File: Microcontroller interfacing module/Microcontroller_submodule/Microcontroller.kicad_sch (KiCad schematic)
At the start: 7 parts, among them U1 STM32F051C6Tx, Y1 8MHz

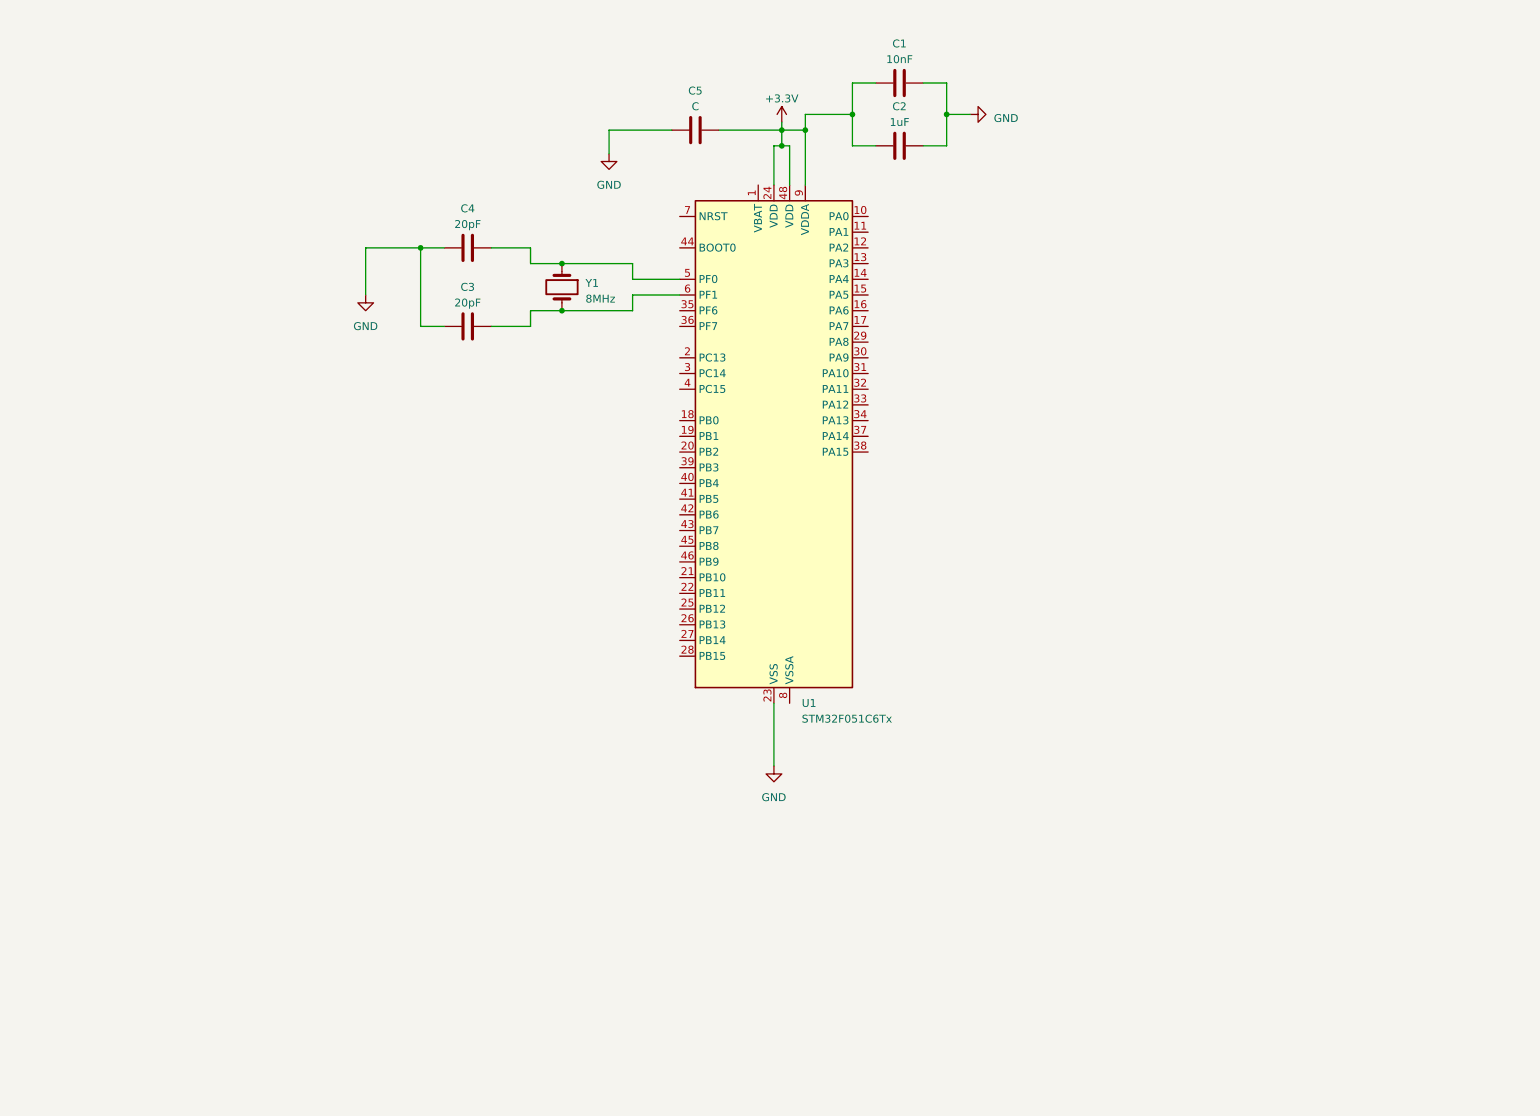
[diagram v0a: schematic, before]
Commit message: Assignment 2 microcontroller sub-module complete
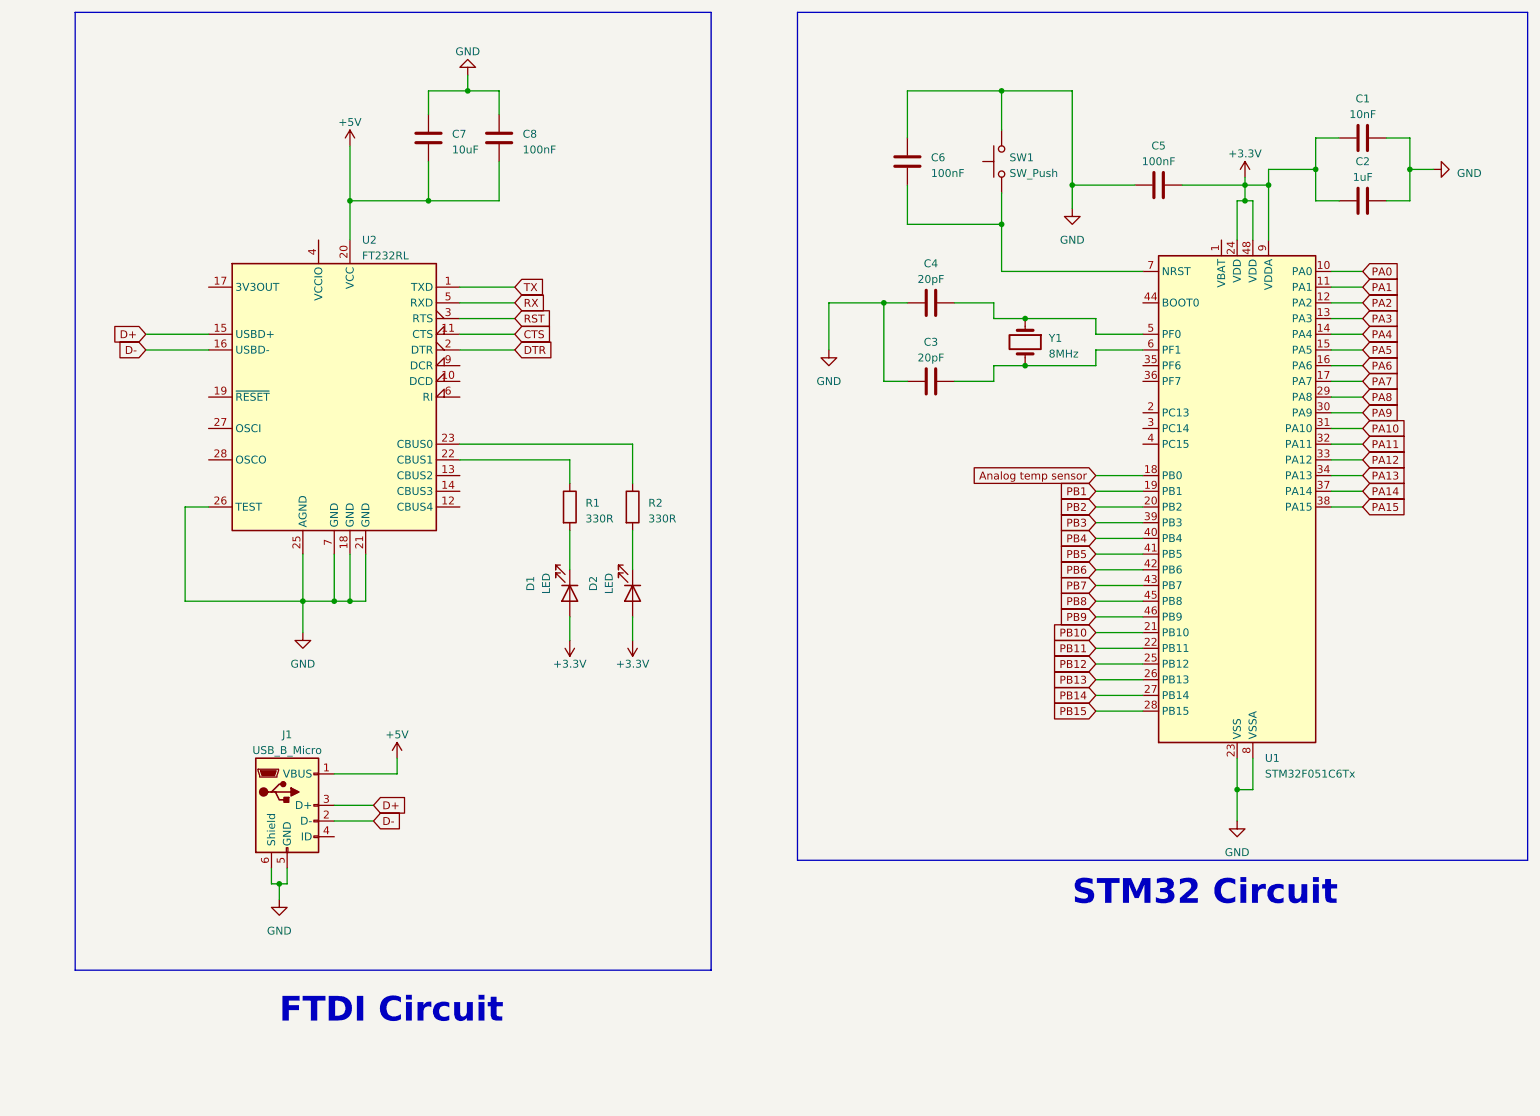
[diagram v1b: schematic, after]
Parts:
- added C6, C8: 100nF, symbol Device:C
- added C7: 10uF, symbol Device:C
- added D1, D2: LED, symbol Device:LED
- added J1: USB_B_Micro, symbol Connector:USB_B_Micro
- added R1, R2: 330R, symbol Device:R
- added SW1: SW_Push, symbol Switch:SW_Push
- added U2: FT232RL, Package_SO:SSOP-28_5.3x10.2mm_P0.65mm, symbol Interface_USB:FT232RL
- C1: Extended part (none) -> 0; JLCPCB Part no: (none) -> C49678; Package (none) -> 0805; Price per unit (none) -> 0.0046; Total price (none) -> 0.0046
- C2: Extended part (none) -> 0; JLCPCB Part no: (none) -> C28323; Package (none) -> 0805; Price per unit (none) -> 0.0087; Total price (none) -> 0.0087
- C3, C4: Extended part (none) -> 0; JLCPCB Part no: (none) -> C107145; Package (none) -> 0805; Price per unit (none) -> 0.0059; Total price (none) -> 0.0118
- C5: value C -> 100nF; Extended part (none) -> 0; JLCPCB Part no: (none) -> C49678; Package (none) -> 0805; Price per unit (none) -> 0.0046; Total price (none) -> 0.0138
- Y1: Extended part (none) -> 0; JLCPCB Part no: (none) -> C12674; Package (none) -> SMD; Price per unit (none) -> 0.0864; Total price (none) -> 0.0864
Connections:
- net +3.3V: now also D1.2 (A), D2.2 (A)
- net GND: now also U1.8 (VSSA), C6.1, C7.1, C8.1, J1.5 (GND), J1.6 (Shield), SW1.2, U2.18 (GND), U2.21 (GND), U2.25 (AGND), U2.26 (TEST), U2.7 (GND)
- net PA0: now reaches U1.10 (PA0)
- net PA1: now reaches U1.11 (PA1)
- net PA2: now reaches U1.12 (PA2)
- net PA3: now reaches U1.13 (PA3)
- net PA4: now reaches U1.14 (PA4)
- net PA5: now reaches U1.15 (PA5)
- net PA6: now reaches U1.16 (PA6)
- net PA7: now reaches U1.17 (PA7)
- net Analog temp sensor: now reaches U1.18 (PB0)
- net PB1: now reaches U1.19 (PB1)
- net PB2: now reaches U1.20 (PB2)
- net PB10: now reaches U1.21 (PB10)
- net PB11: now reaches U1.22 (PB11)
- net PB12: now reaches U1.25 (PB12)
- net PB13: now reaches U1.26 (PB13)
- net PB14: now reaches U1.27 (PB14)
- net PB15: now reaches U1.28 (PB15)
- net PA8: now reaches U1.29 (PA8)
- net PA9: now reaches U1.30 (PA9)
- net PA10: now reaches U1.31 (PA10)
- net PA11: now reaches U1.32 (PA11)
- net PA12: now reaches U1.33 (PA12)
- net PA13: now reaches U1.34 (PA13)
- net PA14: now reaches U1.37 (PA14)
- net PA15: now reaches U1.38 (PA15)
- net PB3: now reaches U1.39 (PB3)
- net PB4: now reaches U1.40 (PB4)
- net PB5: now reaches U1.41 (PB5)
- net PB6: now reaches U1.42 (PB6)
- net PB7: now reaches U1.43 (PB7)
- net PB8: now reaches U1.45 (PB8)
- net PB9: now reaches U1.46 (PB9)
- net at U1.7 (NRST): now also C6.2, SW1.1
- new net: R1.1, U2.22 (CBUS1)
- new net: D1.1 (K), R1.2
- new net: R2.1, U2.23 (CBUS0)
- new net: D2.1 (K), R2.2
- new net +5V: C7.2, C8.2, J1.1 (VBUS), U2.20 (VCC)
- new net CTS: U2.11 (CTS)
- new net D+: J1.3 (D+), U2.15 (USBD+)
- new net D-: J1.2 (D-), U2.16 (USBD-)
- new net DTR: U2.2 (DTR)
- new net RST: U2.3 (RTS)
- new net RX: U2.5 (RXD)
- new net TX: U2.1 (TXD)
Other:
- note added: "FTDI Circuit"
- note added: "STM32 Circuit"
- title: (none) -> Design Project Microcontroller schematic
- moved on the sheet: C1, C2, C3, C4, C5, U1, Y1

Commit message: assignment wk4 update
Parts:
- added J2: Conn_01x10_Pin, symbol Connector:Conn_01x10_Pin
- added U3: CAT24C256, symbol Memory_EEPROM:CAT24C256
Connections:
- net PA10 is gone; now on net TX: U1.31 (PA10)
- net PA9 is gone; now on net RX: U1.30 (PA9)
- net +3.3V: now also U2.4 (VCCIO), U3.8 (VCC)
- net +5V: now also J2.1 (Pin_1)
- net Analog temp sensor: now also J2.2 (Pin_2)
- net GND: now also J2.10 (Pin_10), U3.1 (A0), U3.2 (A1), U3.3 (A2), U3.4 (GND), U3.7 (WP)
- net RX: now also J2.9 (Pin_9)
- net TX: now also J2.8 (Pin_8)
- net Eprom_SLC: now reaches U1.35 (PF6)
- net Eprom_SLC: now also U3.6 (SCL)
- net Eprom_SDA: now reaches U1.36 (PF7)
- net Eprom_SDA: now also U3.5 (SDA)
- net CTS: no longer names the net of U2.11 (CTS)
- net DTR: no longer names the net of U2.2 (DTR)
- net PB10 renamed Temp_Sensor_SLC
- net Temp_Sensor_SLC: now also J2.4 (Pin_4)
- net PB11 renamed Temp_Sensor_SDA
- net Temp_Sensor_SDA: now also J2.3 (Pin_3)
- net RST: no longer names the net of U2.3 (RTS)
- new net Plug_Detect: J2.7 (Pin_7)
- no-connect marks 0 -> 21
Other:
- note added: "Debug Header"
- note added: "Eprom"
- moved on the sheet: J1
